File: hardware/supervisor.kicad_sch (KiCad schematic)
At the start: 10 parts

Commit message: Alpha 1.0.0 Schematic
First Schematic Version for initial checkup
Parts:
- added C? (x2): 100nF, Capacitor_SMD:C_0603_1608Metric_Pad1.08x0.95mm_HandSolder, symbol Device:C
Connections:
- net 3V3_A is gone; now on net +3V3: U?.13 (VDDA/VREF+)
- net 3V3_SYS is gone; now on net +3V3: U?.1 (VBAT), U?.5 (Vio)
- net LED2 is gone; now on net WATCHDOG: U?.21 (PA5)
- net LED3 is gone; now on net AS_CLOSE_SDC: U?.22 (PA6)
- net LED4 is gone; now on net AS_DRIVING_MODE: U?.23 (PA7)
- net SENSOR1 is gone; now on net SENSOR_1: U?.24 (PC4)
- net SENSOR2 is gone; now on net SENSOR_2: U?.25 (PC5)
- net +3V3: now also C?.1, C?.1
- net GND: now also C?.2, C?.2
- net SDC_READY: now also U?.38 (PC7)
- net SENSOR_3: now also U?.37 (PC6)
- net VALVE_1: now also U?.30 (PB11)
- net VALVE_2: now also U?.34 (PB13)
- net EBS LIGHT SIG: now reaches U?.62 (PB9)
- net NRST: now reaches U?.7 (NRST)
- net CLK renamed SWDCLK
- net EN_RELAY: no longer names the net of U?.61 (PB8)
- net LED1: no longer names the net of U?.20 (PA4)
- net SWD renamed SWDIO
- no-connect marks 42 -> 34
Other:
- moved on the sheet: C?, D?, JP?, R?, U?, Y?

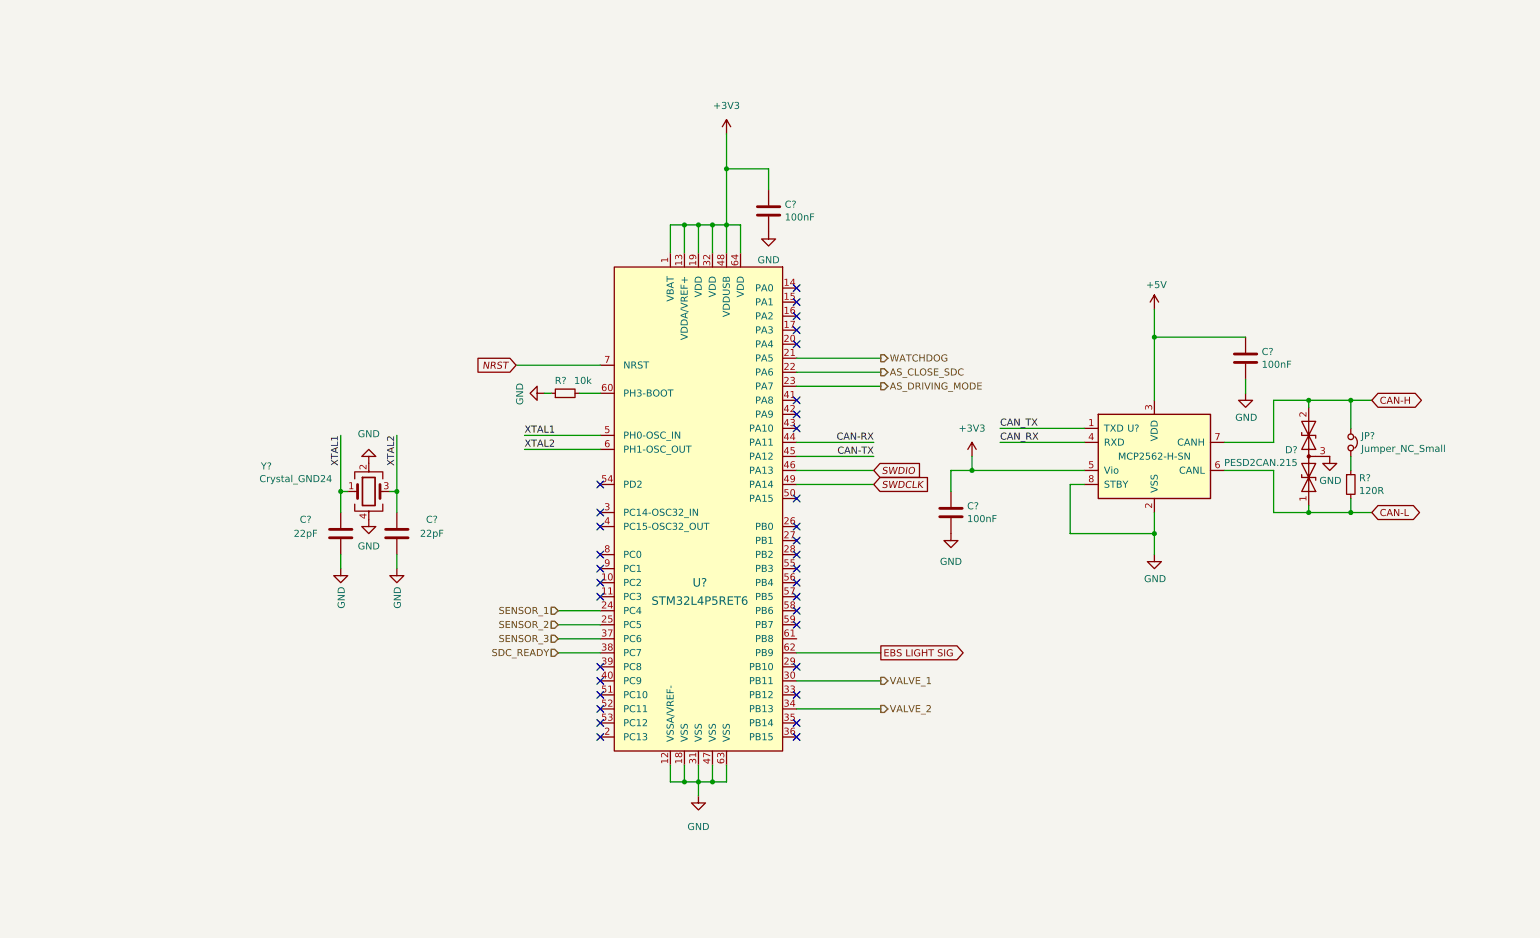
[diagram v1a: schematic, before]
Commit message: Minor changes on v1 schematic
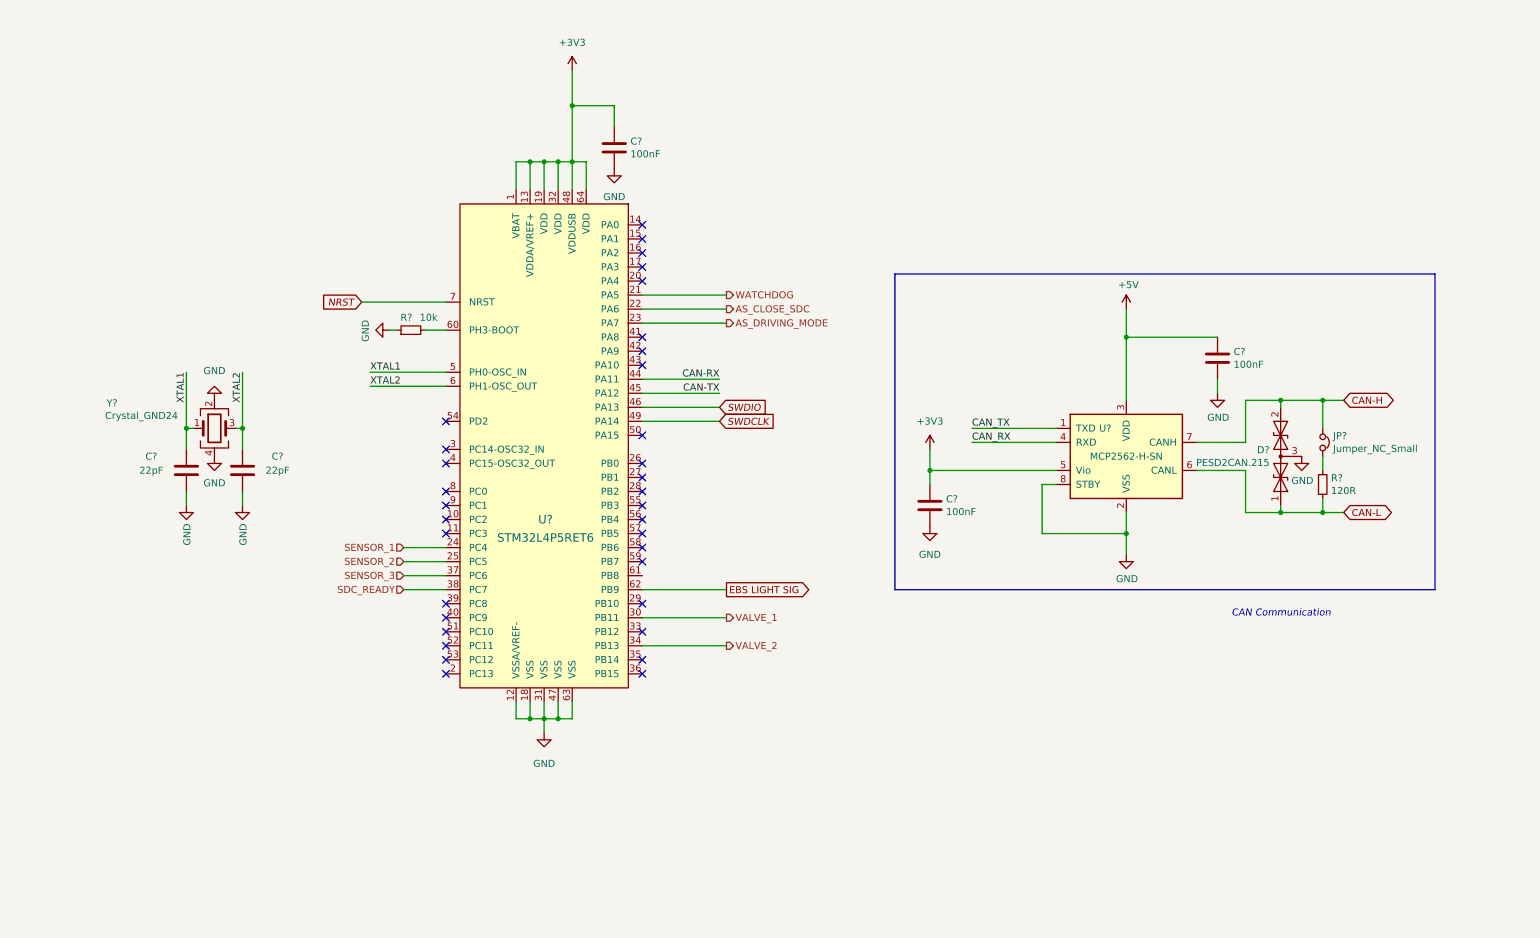
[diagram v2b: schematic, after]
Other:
- note added: "CAN Communication"
- moved on the sheet: C?, D?, JP?, R?, U?, Y?

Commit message: minor schematic cleanup
Fixes before second review
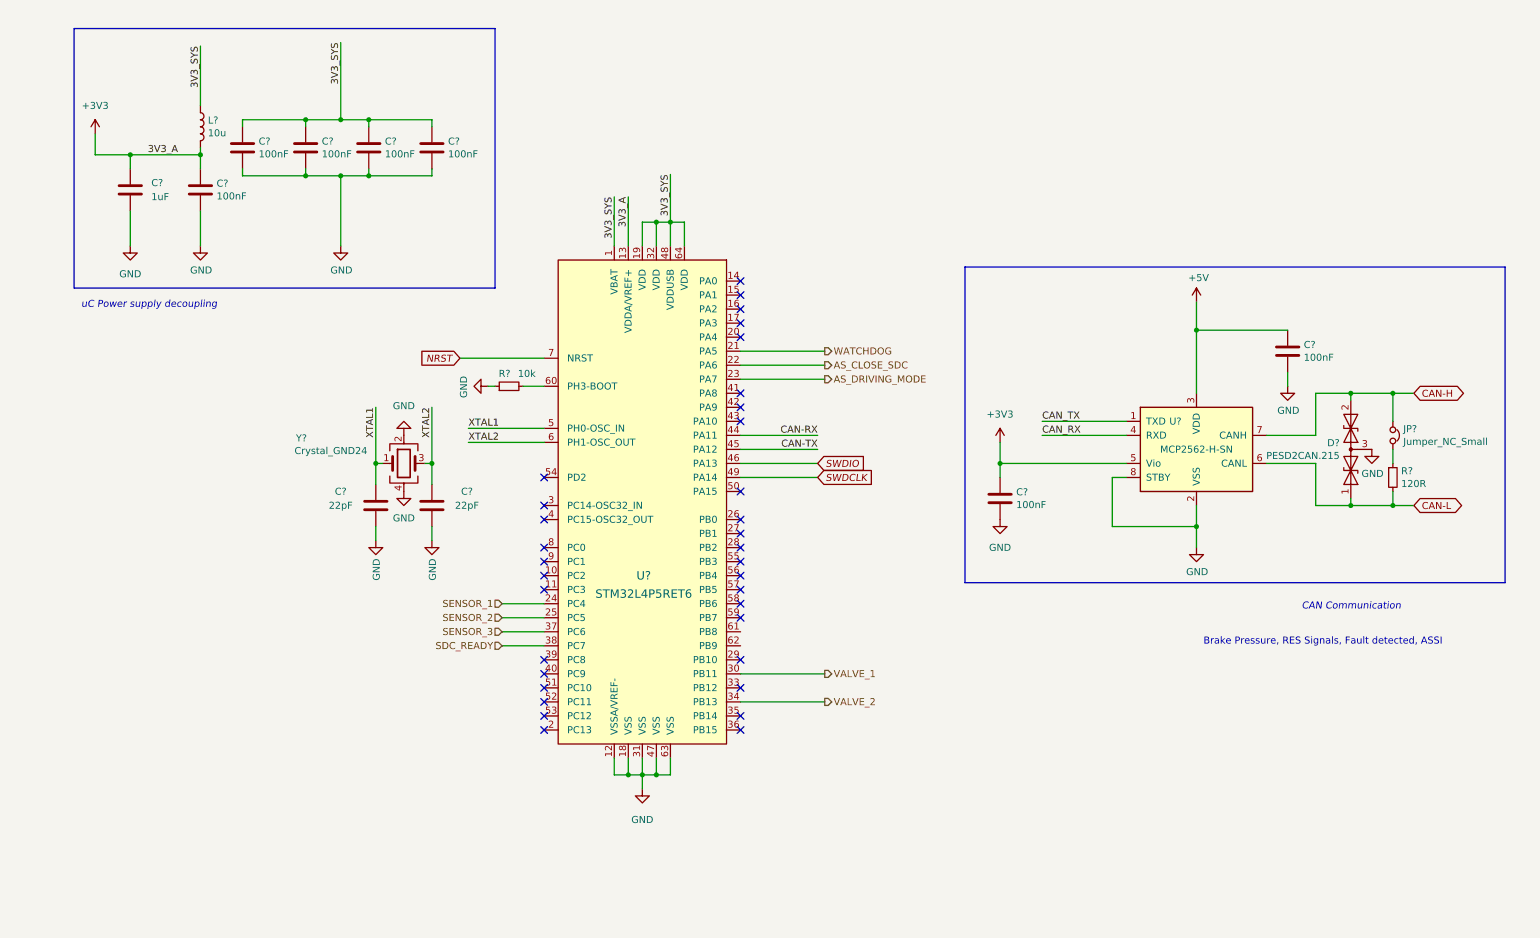
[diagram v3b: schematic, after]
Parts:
- removed C?: 100nF, Capacitor_SMD:C_0603_1608Metric_Pad1.08x0.95mm_HandSolder, symbol Device:C
- added C? (x5): 100nF, Capacitor_SMD:C_0603_1608Metric_Pad1.08x0.95mm_HandSolder, symbol Device:C
- added C?: 1uF, symbol Device:C
- added L?: 10u, Inductor_SMD:L_0805_2012Metric, symbol Device:L
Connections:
- net +3V3: now also C?.1, C?.1, L?.2; no longer U?.1 (VBAT), U?.19 (VDD), U?.32 (VDD), U?.48 (VDDUSB), U?.64 (VDD)
- net GND: now also C?.2, C?.2, C?.2, C?.2, C?.2, C?.2
- net EBS LIGHT SIG: no longer names the net of U?.62 (PB9)
- new net 3V3_SYS: C?.1, C?.1, C?.1, C?.1, L?.1, U?.1 (VBAT), U?.19 (VDD), U?.32 (VDD), U?.48 (VDDUSB), U?.64 (VDD)
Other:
- note added: "Brake Pressure, RES Signals, Fault detected, ASSI"
- note added: "uC Power supply decoupling"
- company: (none) -> PUT Motorsport
- title: (none) -> Autonomus System Brake Control and EBS Supervisor uC
- moved on the sheet: C?, D?, JP?, R?, U?, Y?

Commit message: Schematic ready for second review
Cleaned up, numerated, added footprints, JW notes considered
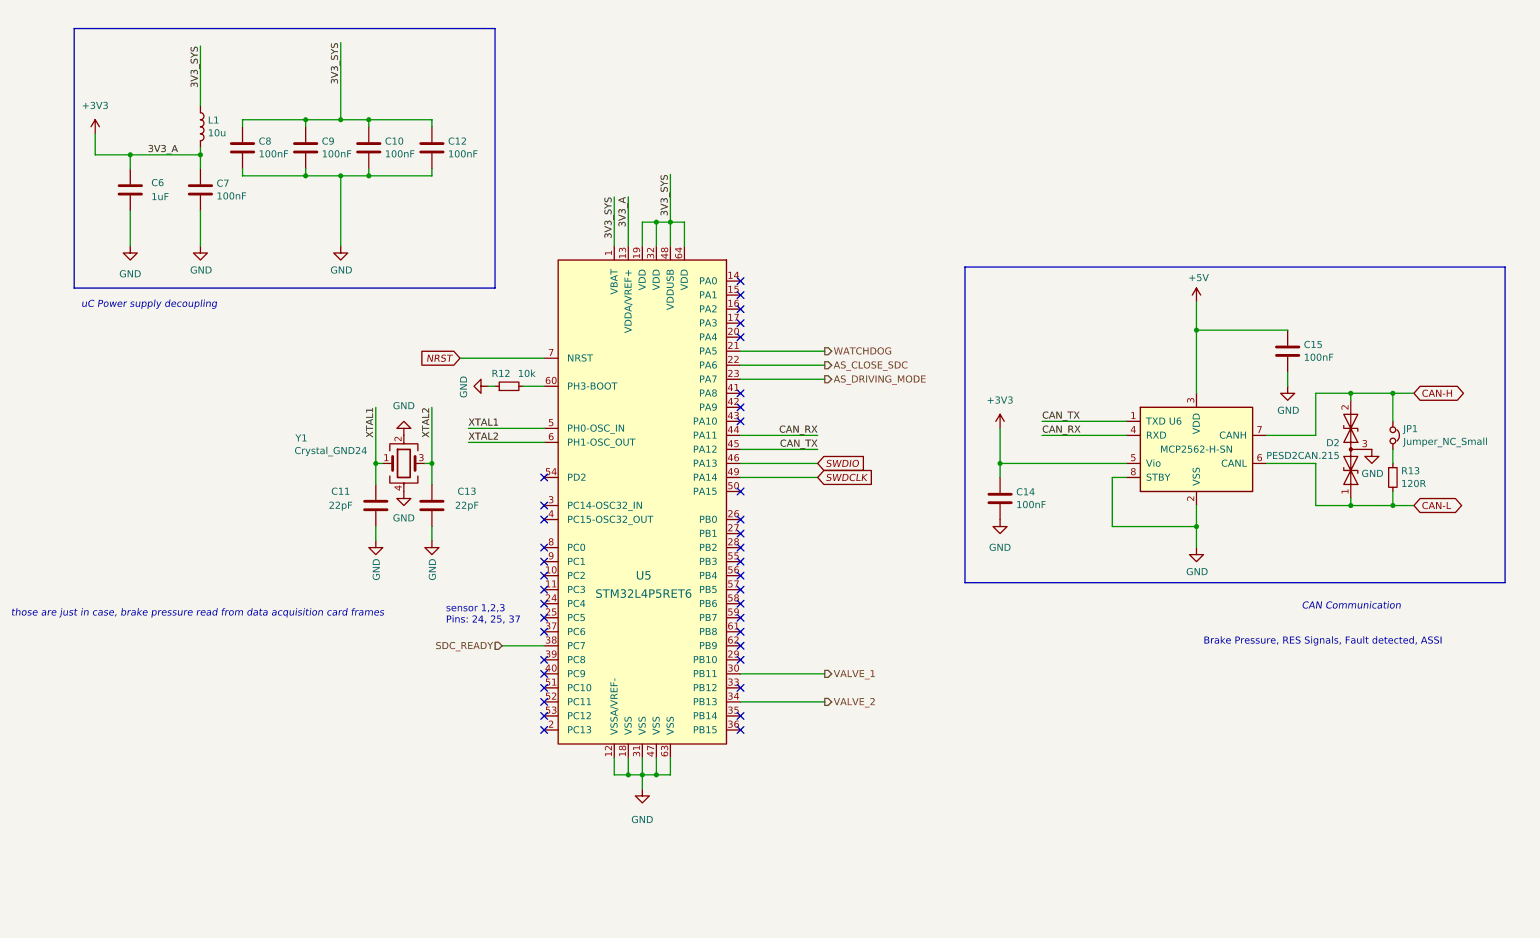
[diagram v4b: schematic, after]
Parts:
- C6: renamed from C?; footprint (none) -> Capacitor_SMD:C_0201_0603Metric_Pad0.64x0.40mm_HandSolder
- gave numbers to parts that had none: 17
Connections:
- net CAN-RX is gone; now on net CAN_RX: U5.44 (PA11)
- net CAN-TX is gone; now on net CAN_TX: U5.45 (PA12)
- net SENSOR_1: no longer names the net of U5.24 (PC4)
- net SENSOR_2: no longer names the net of U5.25 (PC5)
- net SENSOR_3: no longer names the net of U5.37 (PC6)
- no-connect marks 34 -> 39
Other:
- note added: "sensor 1,2,3 Pins: 24, 25, 37"
- note added: "those are just in case, brake pressure read from data acquisition card frames"
